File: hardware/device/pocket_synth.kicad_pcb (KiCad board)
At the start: 6 copper layers, 74 x 138 mm, 131 parts, among them IC2 IS42S16160J-7BLI, J1 POT_CONN, J10 HP_OUT, J2 USB, J3 MICRO_SD, J4 EXPANSION, J5 AUDIO_EXP, J8 LINE_OUT, J9 LINE_IN, SW1 TRIG1, SW10 TRIG10, SW11 TRIG11, SW12 TRIG12, SW13 TRIG13, SW14 TRIG14, SW15 TRIG15, SW16 TRIG16, SW17 KMR221NGLFS, SW18 HELP, SW19 LEFT_BTN, SW2 TRIG2, SW20 RIGHT_BTN, SW3 TRIG3, SW4 TRIG4, SW5 TRIG5, SW6 TRIG6, SW7 TRIG7, SW8 TRIG8, SW9 TRIG9, U10 TRIG9, U11 TRIG13, U12 TRIG10, U13 TRIG14, U14 TRIG11, U15 TRIG15, U16 TRIG12, U17 TRIG16, U18 STM32H743ZIT6, U19 ER-TFT024IPS-3, U2 TRIG1, U20 TPS62A02DRL, U21 TPS560200, U22 MAX17261xxTD, U23 BQ21040DBV, U24 MIC, U25 TCA8418RTWR, U26 FUSB303BTMX, U27 FUSB302B01MPX, U29 NAU88C22YG, U3 TRIG2, U4 TRIG3, U5 TRIG4, U6 TRIG8, U7 TRIG7, U8 TRIG6, U9 TRIG5

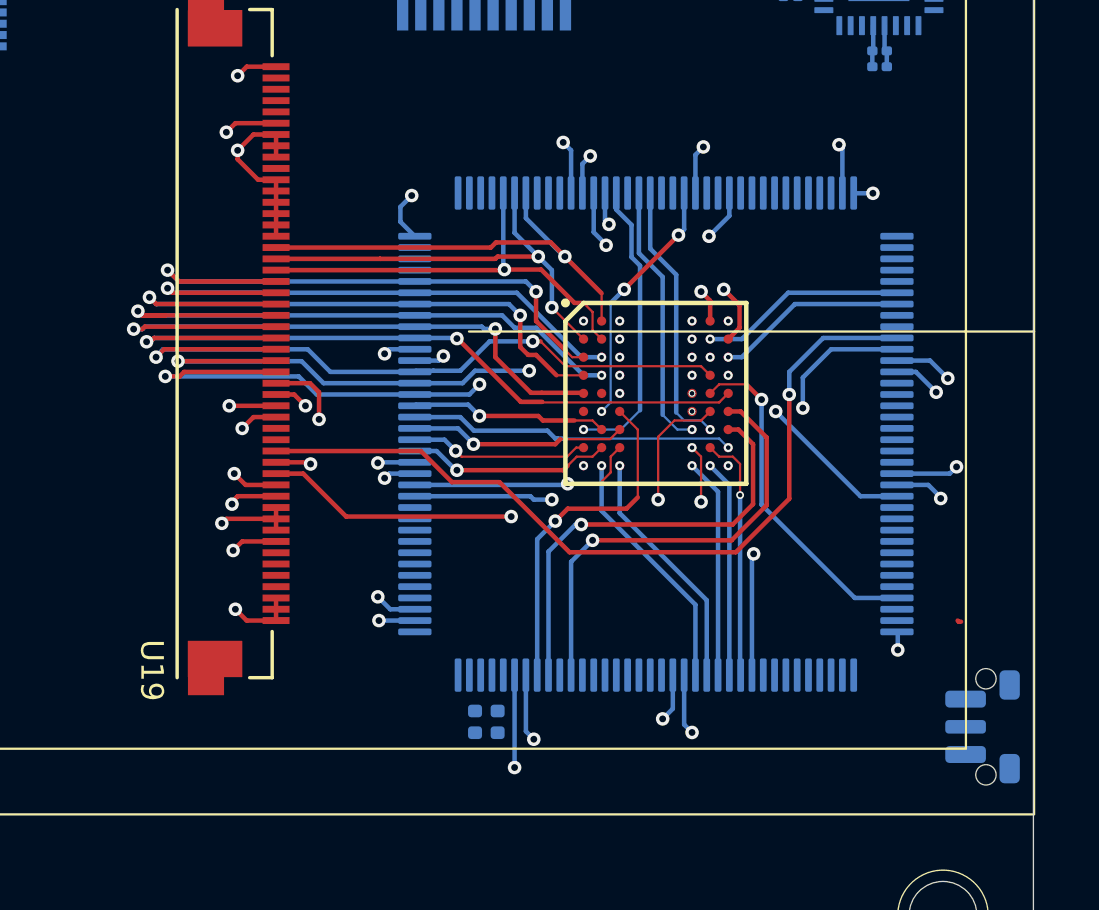
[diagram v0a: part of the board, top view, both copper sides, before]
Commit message: chore: shift STM32 closer to FPC
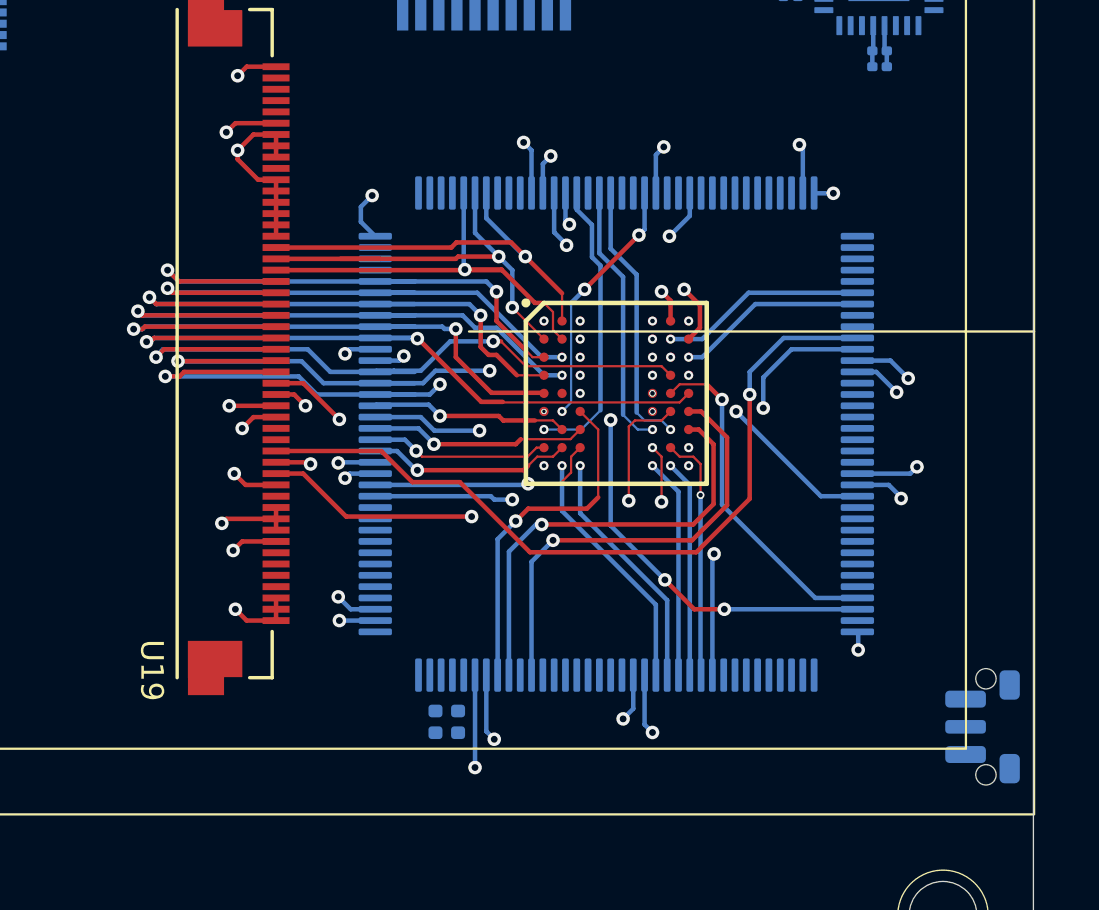
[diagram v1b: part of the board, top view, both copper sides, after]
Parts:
- moved C88 1.75 mm to (77.5, 83.5)
- moved C89 1.75 mm to (78.5, 83.5)
- moved IC2 1.75 mm to (85.5, 69.0)
- moved U18 1.75 mm to (85.5, 70.8)
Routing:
- net /Display/FMC.DQMH: track 0.00 -> 20.2 mm, vias 0 -> 4
- net /Display/FMC.D3: track 32.1 -> 29.6 mm
- net /Display/DISPLAY_TE: track 2.15 -> 0.00 mm, vias 1 -> 0
- net /Display/FMC.D15: track 20.2 -> 18.4 mm
- net /Display/FMC.D0: track 32.3 -> 30.6 mm
- net /Display/FMC.A0: track 31.7 -> 29.9 mm
- net /Display/FMC.NOE: track 36.5 -> 34.8 mm
- net /Display/FMC.NE1: track 35.1 -> 33.3 mm
- net /Display/FMC.D2: track 30.1 -> 28.4 mm
- net /Display/FMC.D1: track 34.0 -> 32.3 mm
- net /Display/FMC.NWE: track 37.2 -> 35.4 mm
- net /Display/FMC.D9: track 28.9 -> 27.9 mm
- net /Display/FMC.A10: vias 1 -> 2

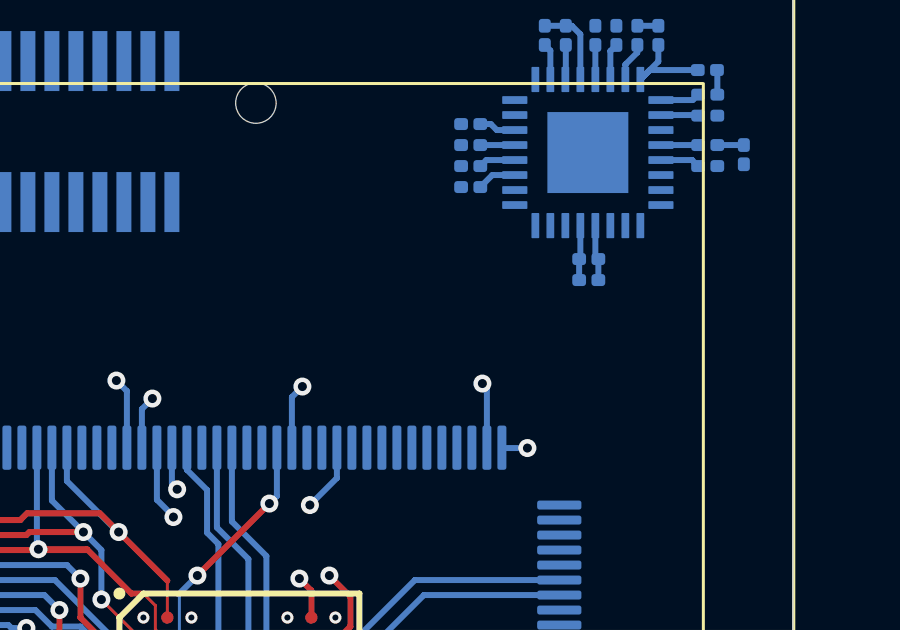
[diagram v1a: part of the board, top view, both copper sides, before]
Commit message: feat: add BMPU debug connector
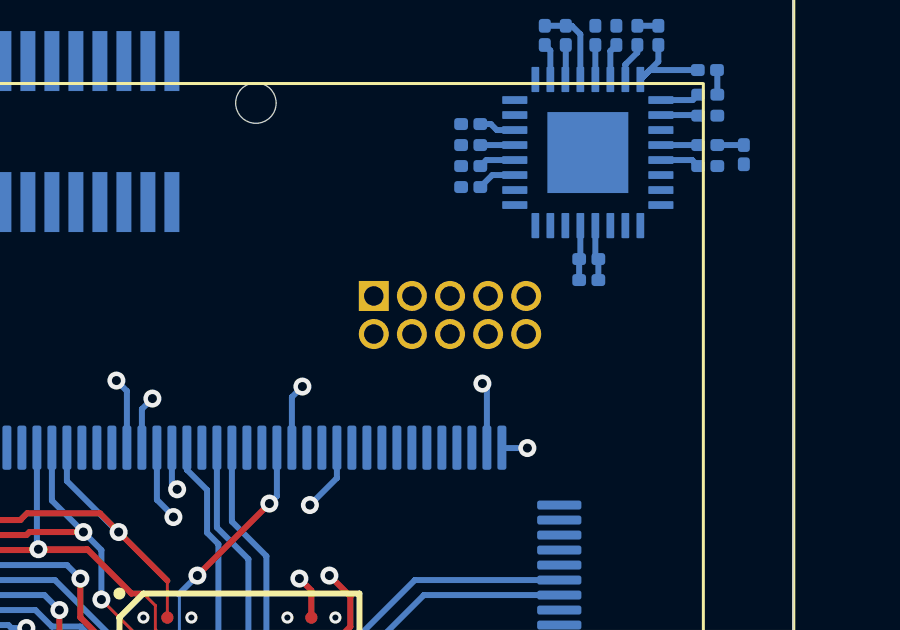
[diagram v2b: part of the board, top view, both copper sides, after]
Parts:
- added U1: BMDU, Connector_PinHeader_1.27mm:PinHeader_2x05_P1.27mm_Vertical, B.Cu at (90.0, 55.0)
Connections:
- U18 pad 105: unconnected-(U18A-PA13-Pad105) -> /MCU/SWD_SWDIO
- U18 pad 109: unconnected-(U18A-PA14-Pad109) -> /MCU/SWD_SWCLK
- U18 pad 133: unconnected-(U18B-PB3-Pad133) -> /MCU/SWD_SWO
